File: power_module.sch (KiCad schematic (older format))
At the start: 29 parts, among them J1 USB_B, J2 VOUT, J3 CONN_01X03, J4 CONN_01X06, Q1 Q_NMOS_GSD, U1 ATTINY24A-SSU

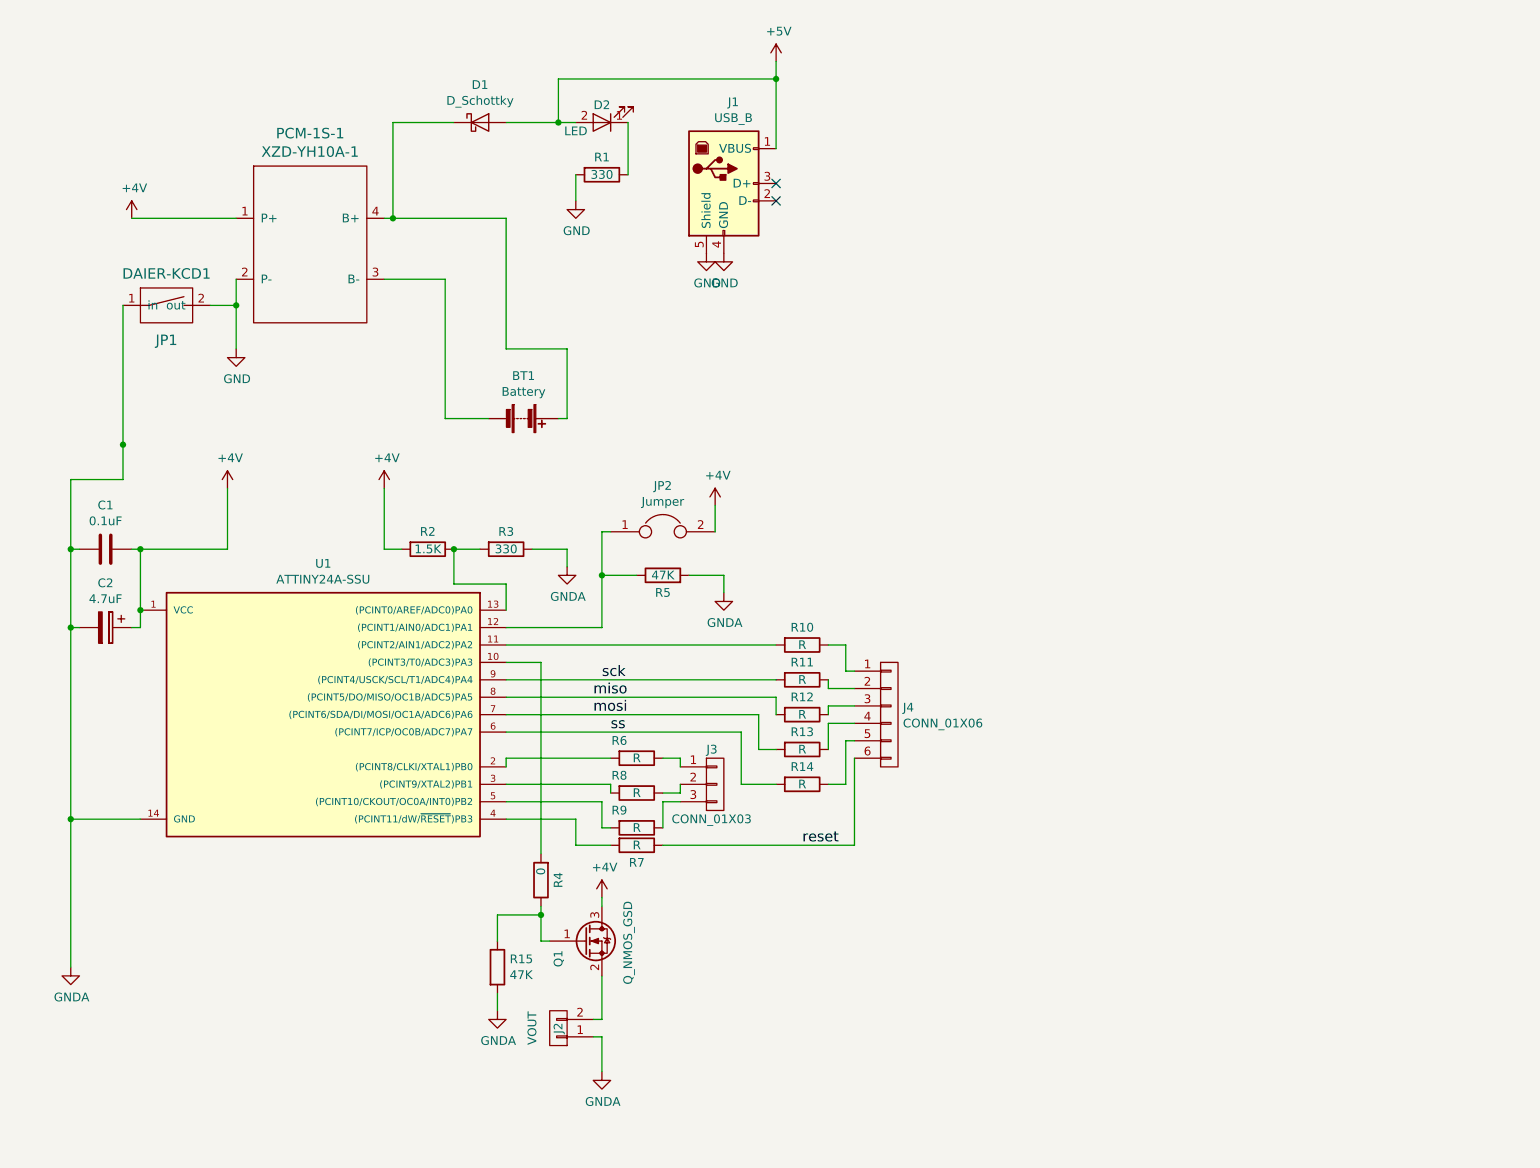
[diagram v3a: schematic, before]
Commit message: Make it one side
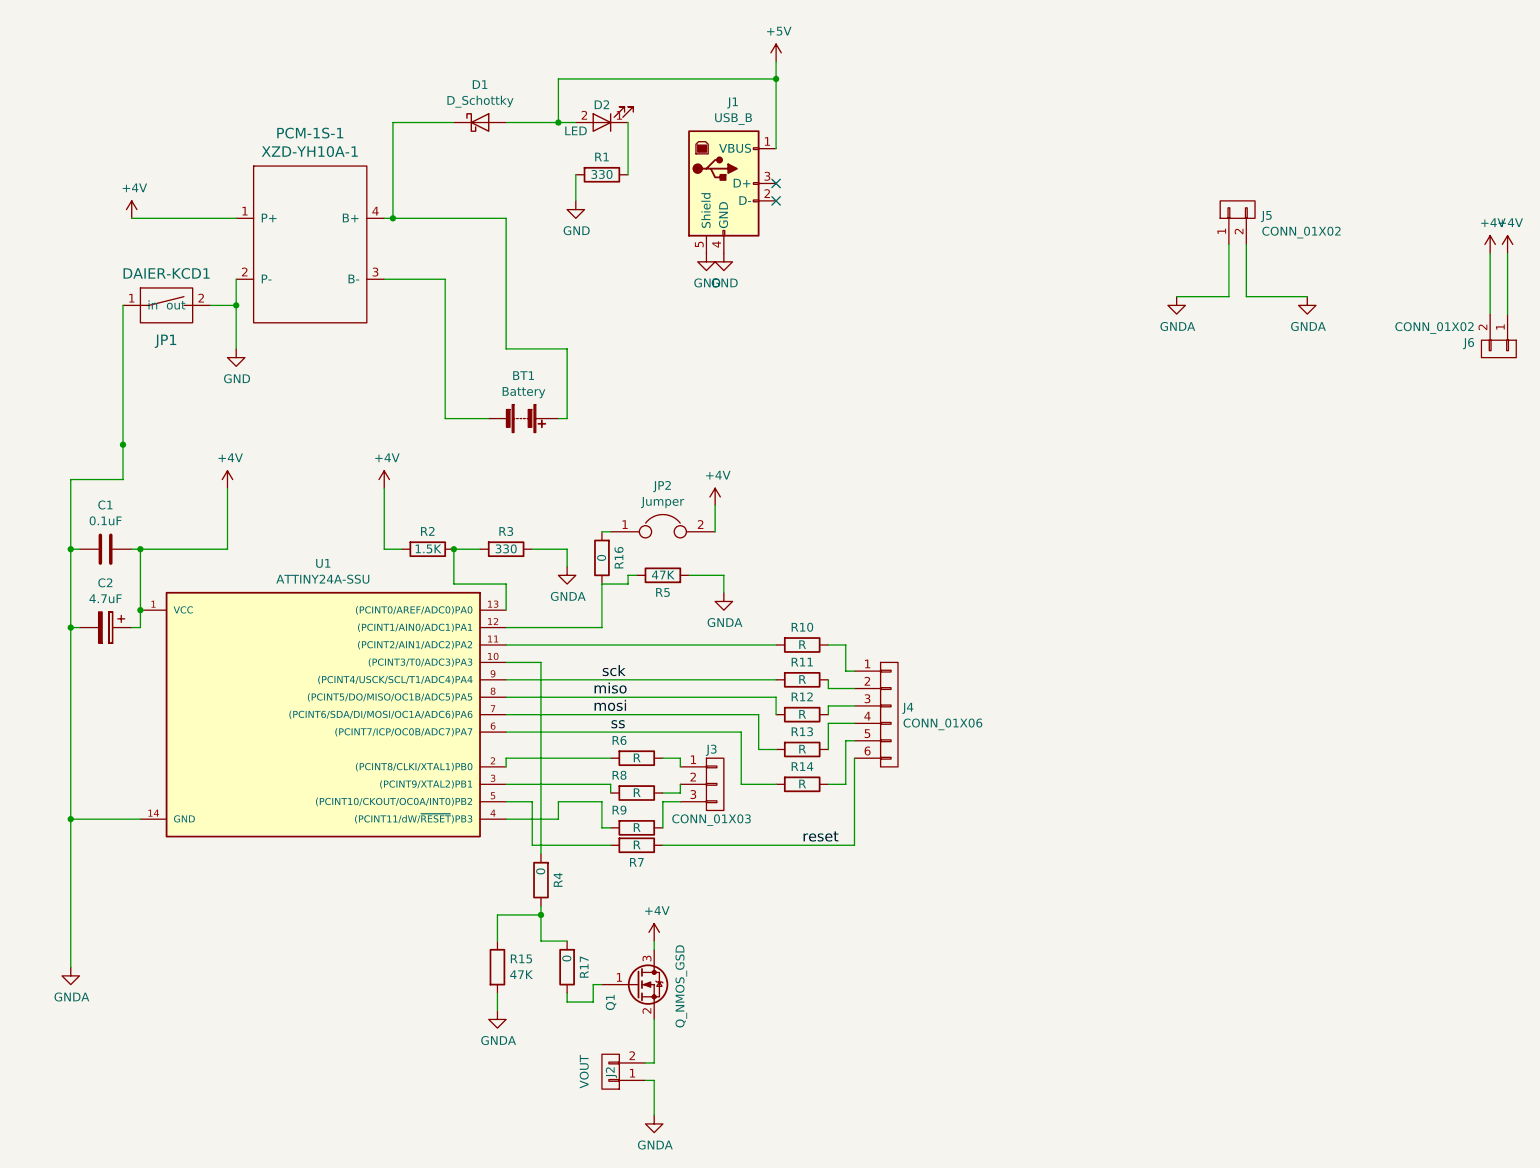
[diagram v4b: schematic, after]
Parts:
- added J5, J6: CONN_01X02, Resistors_SMD:R_2512, symbol CONN_01X02
- added R16: 0, Resistors_SMD:R_1206, symbol R
- added R17: 0, Resistors_SMD:R_2512, symbol R
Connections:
- net +4V: now also J6.1 (P1), J6.2 (P2)
- net GNDA: now also J5.1 (P1), J5.2 (P2)
- net at R5.1, U1.12 ((PCINT1/AIN0/ADC1)PA1): now also R16.1; no longer JP2.1
- net at U1.4 ((PCINT11/dW/~RESET~)PB3): now also R9.2; no longer R7.2
- net at U1.5 ((PCINT10/CKOUT/OC0A/INT0)PB2): now also R7.2; no longer R9.2
- net at R15.1, R4.1: now also R17.2; no longer Q1.1 (G)
- new net: JP2.1, R16.2
- new net: Q1.1 (G), R17.1
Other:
- moved on the sheet: J2, Q1

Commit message: Поправил схему н-канального транзистора, обновил дорожки на плате, удалил не нужные файлы, поправил посадочные места для выключателя, поправил посадочное место для батареии 18650
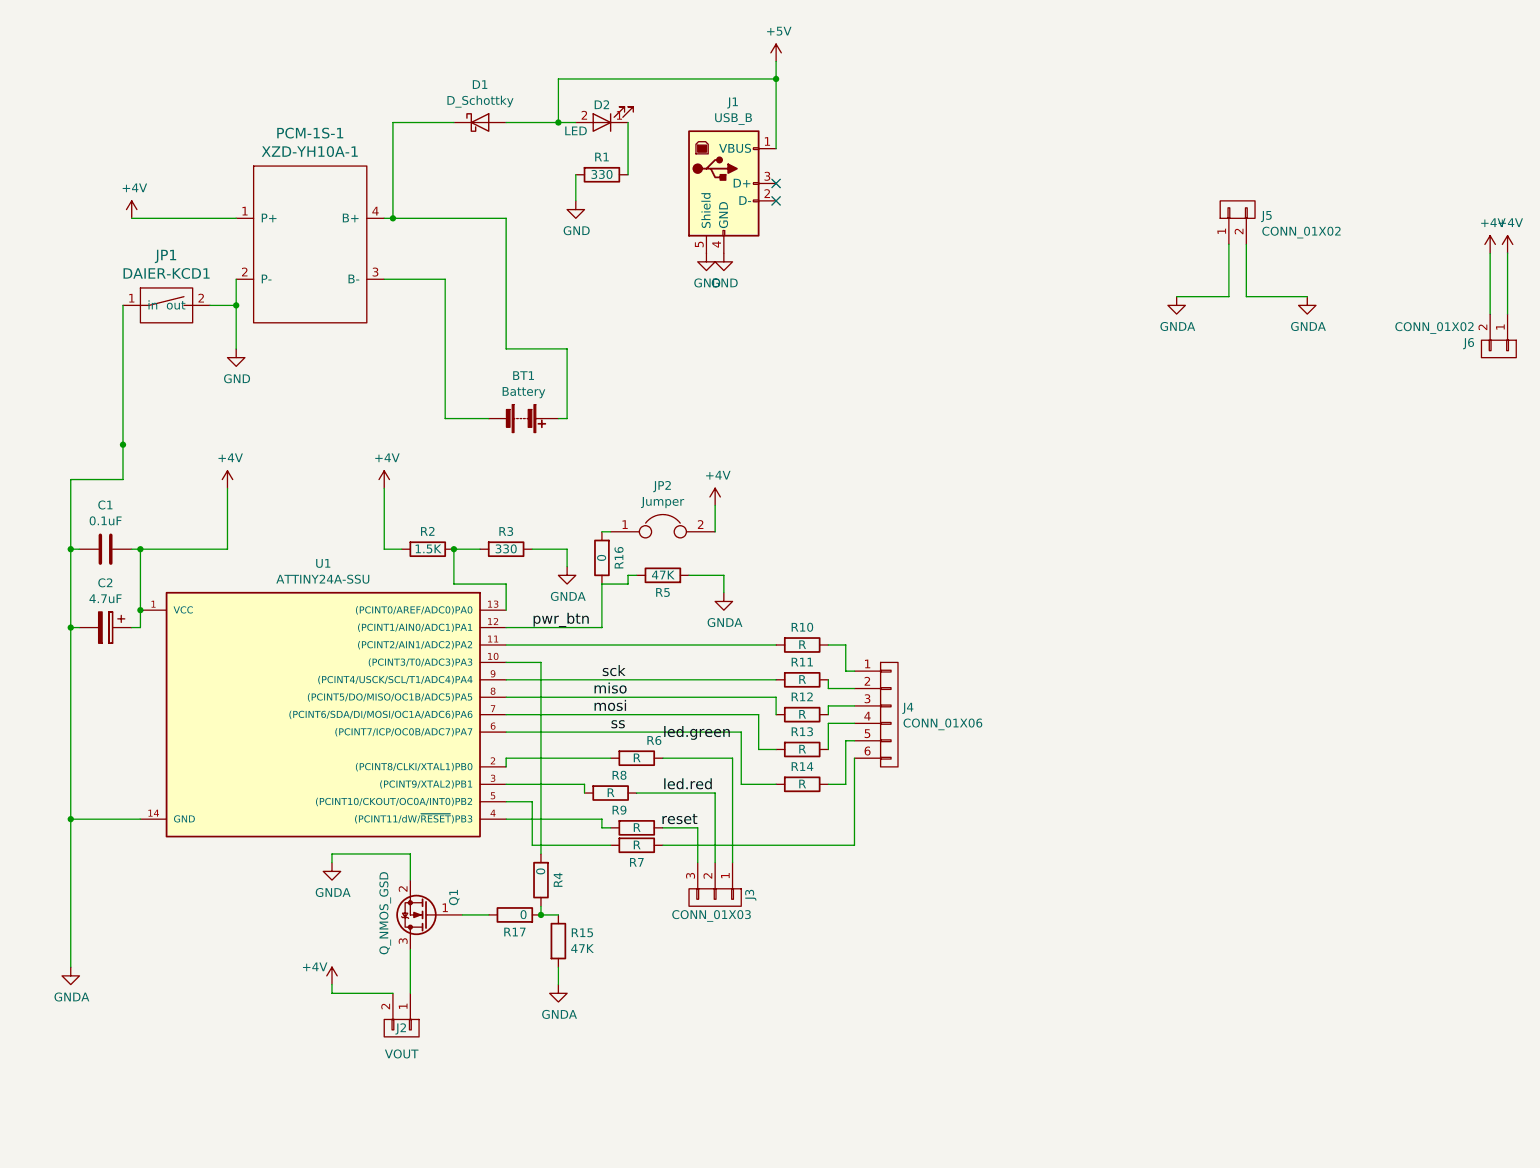
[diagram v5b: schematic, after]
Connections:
- net +4V: now also J2.2 (P2); no longer Q1.3 (D)
- net GNDA: now also Q1.2 (S); no longer J2.1 (P1)
- net reset: now also J3.3 (P3), R9.1; no longer J4.6 (P6), R7.1
- net pwr_btn: now reaches R16.1, R5.1, U1.12 ((PCINT1/AIN0/ADC1)PA1)
- net led.red: now reaches J3.2 (P2), R8.1
- new net: J2.1 (P1), Q1.3 (D)
- new net: J4.6 (P6), R7.1
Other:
- moved on the sheet: J2, J3, Q1, R15, R17, R8

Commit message: Мелкие поправки по плате
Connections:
- net led.green: now also J3.1 (P1), R6.1
- net ss: now also R7.2, U1.5 ((PCINT10/CKOUT/OC0A/INT0)PB2); no longer R14.2, U1.6 ((PCINT7/ICP/OC0B/ADC7)PA7)
- new net: R14.2, U1.6 ((PCINT7/ICP/OC0B/ADC7)PA7)
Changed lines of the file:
@@
 Text Label 5250 5900 2    60   ~ 0
 reset
-Text Label 4750 5350 0    60   ~ 0
+Text Label 4150 5750 0    60   ~ 0
 ss
 $Comp
@@
 Text Label 4300 4750 0    60   ~ 0
 pwr_btn
-Text Label 5050 5400 0    60   ~ 0
+Text Label 5050 5500 0    60   ~ 0
 led.green
 Text Label 5050 5700 0    60   ~ 0
